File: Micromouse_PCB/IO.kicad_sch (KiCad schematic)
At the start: 22 parts, among them J4 Power, J5 ALARM, Q11 Q_NMOS_GSD, SW1 Slide switch, SW2 SW_Push, SW3 SW_Push

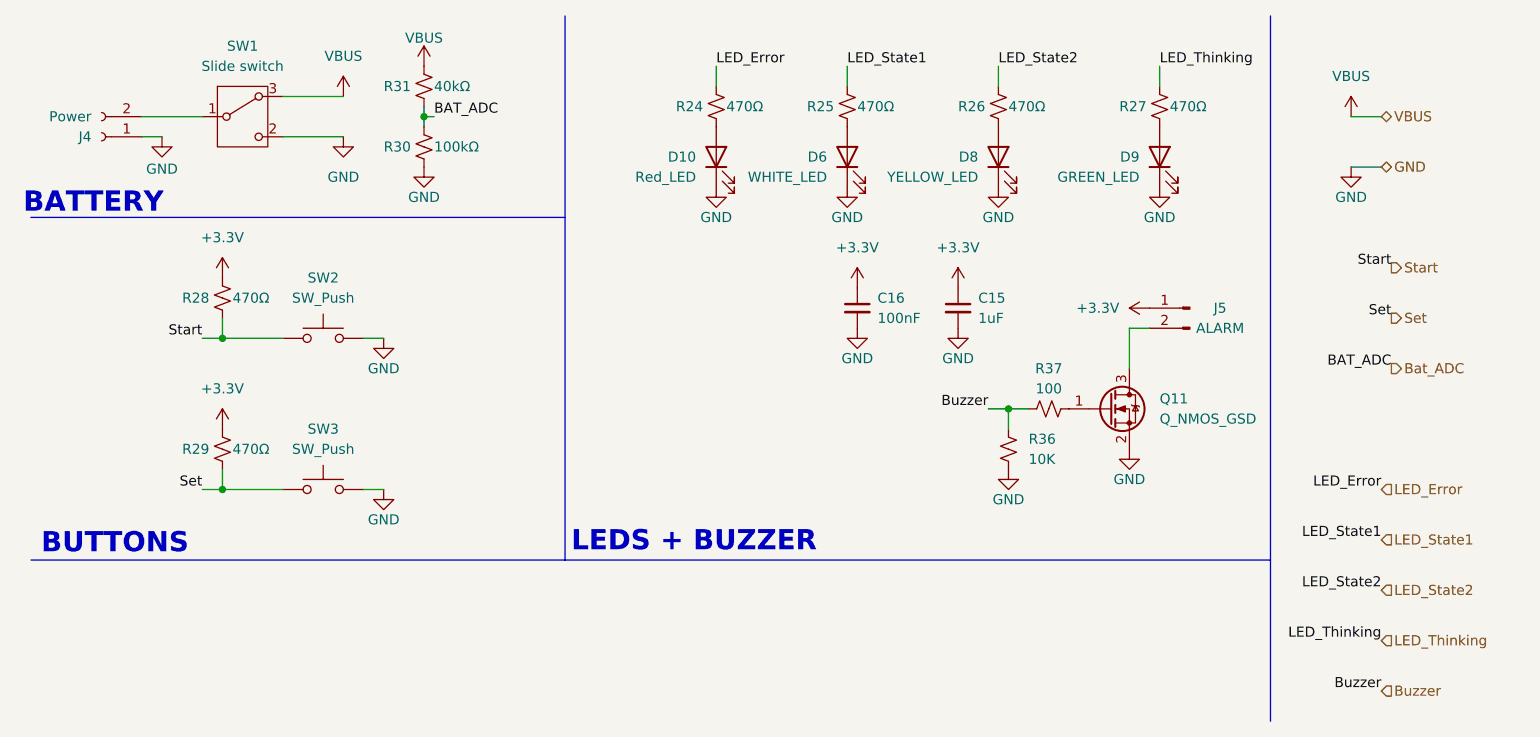
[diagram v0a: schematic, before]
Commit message: Schematic done
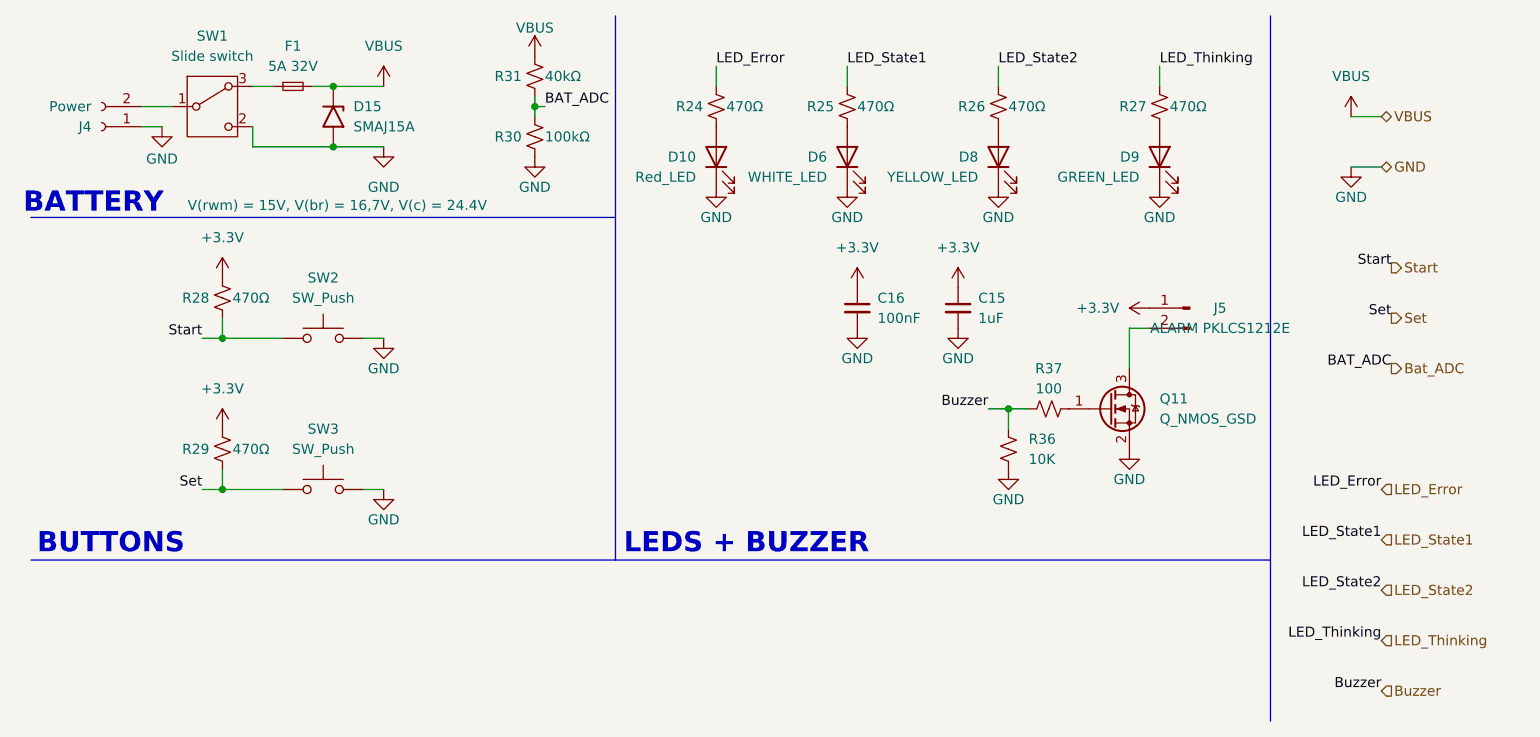
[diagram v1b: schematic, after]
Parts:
- added D15: SMAJ15A, Diode_SMD:D_SMA, symbol Diode:SMAJ15A
- added F1: 5A 32V, Fuse:Fuse_0603_1608Metric, symbol Device:Fuse_Small
- J5: value ALARM -> ALARM PKLCS1212E; Part # SMT-0540-S-R -> (none)
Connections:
- net GND: now also D15.2 (A2)
- net VBUS: now also D15.1 (A1), F1.2; no longer SW1.3 (A)
- new net: F1.1, SW1.3 (A)
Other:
- moved on the sheet: J4, R30, R31, SW1

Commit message: Placement 75% done on PCB
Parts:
- SW1: footprint UCIRP-KiCAD-Lib:Horizontal_Slide_Swiitch SK12D07VG4NSPA_CNK -> Button_Switch_THT:SW_Slide-03_Wuerth-WS-SLTV_10x2.5x6.4_P2.54mm
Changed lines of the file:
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@@
 			)
 		)
-		(property "Footprint" "UCIRP-KiCAD-Lib:Horizontal_Slide_Swiitch SK12D07VG4NSPA_CNK"
+		(property "Footprint" "Button_Switch_THT:SW_Slide-03_Wuerth-WS-SLTV_10x2.5x6.4_P2.54mm"
 			(at 35.56 34.29 0)
 			(effects

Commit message: PCB Done, need review now
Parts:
- J4: value Power -> Power XT30UPB-M; footprint Connector_AMASS:AMASS_XT30U-F_1x02_P5.0mm_Vertical -> Connector_AMASS:AMASS_XT30UPB-F_1x02_P5.0mm_Vertical
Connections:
- net +3.3V renamed +3V3
- net LED_Error renamed LED_Thinking1
- net LED_Thinking renamed LED_Thinking2
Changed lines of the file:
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@@
 		)
 	)
-	(label "LED_Thinking"
+	(label "LED_Thinking2"
 		(at 154.94 19.05 0)
 		(effects
@@
 		)
 	)
-	(label "LED_Thinking"
+	(label "LED_Thinking1"
+		(at 182.88 72.39 180)
+		(effects
+			(font
+				(size 1.27 1.27)
+			)
+			(justify right bottom)
+		)
+	)
+	(label "LED_Thinking2"
 		(at 182.88 91.44 180)
 		(effects
@@
 		)
 	)
-	(label "LED_Error"
-		(at 182.88 72.39 180)
-		(effects
-			(font
-				(size 1.27 1.27)
-			)
-			(justify right bottom)
-		)
-	)
 	(label "BAT_ADC"
 		(at 77.47 24.13 0)
@@
 		)
 	)
-	(label "LED_Error"
+	(label "LED_Thinking1"
 		(at 99.06 19.05 0)
 		(effects
@@
 		)
 	)
-	(hierarchical_label "LED_Thinking"
+	(hierarchical_label "LED_Thinking2"
 		(shape input)
 		(at 182.88 91.44 0)
@@
 		)
 	)
-	(hierarchical_label "LED_Error"
+	(hierarchical_label "LED_Thinking1"
 		(shape input)
 		(at 182.88 72.39 0)
@@
 		(on_board yes)
 		(dnp no)
-		(fields_autoplaced yes)
 		(property "Reference" "#PWR093"
 			(at 129.54 50.8 0)
@@
 			)
 		)
-		(property "Value" "+3.3V"
-			(at 129.54 41.91 0)
+		(property "Value" "+3V3"
+			(at 126.746 42.926 0)
 			(effects
 				(font
 					(size 1.27 1.27)
 				)
+				(justify left)
 			)
 		)
@@
 		(on_board yes)
 		(dnp no)
-		(fields_autoplaced yes)
 		(property "Reference" "#PWR099"
 			(at 36.83 49.53 0)
@@
 			)
 		)
-		(property "Value" "+3.3V"
-			(at 36.83 40.64 0)
+		(property "Value" "+3V3"
+			(at 33.782 41.91 0)
 			(effects
 				(font
 					(size 1.27 1.27)
 				)
+				(justify left)
 			)
 		)
@@
 		(on_board yes)
 		(dnp no)
-		(fields_autoplaced yes)
 		(property "Reference" "#PWR095"
 			(at 116.84 50.8 0)
@@
 			)
 		)
-		(property "Value" "+3.3V"
-			(at 116.84 41.91 0)
+		(property "Value" "+3V3"
+			(at 113.792 42.926 0)
 			(effects
 				(font
 					(size 1.27 1.27)
 				)
+				(justify left)
 			)
 		)
@@
 		(dnp no)
 		(property "Reference" "J5"
-			(at 162.56 49.53 0)
+			(at 162.306 41.402 0)
 			(effects
 				(font
@@
 		)
 		(property "Value" "ALARM PKLCS1212E"
-			(at 162.56 52.07 0)
+			(at 158.496 43.942 0)
 			(effects
 				(font
@@
 		(dnp no)
 		(property "Reference" "J4"
-			(at 20.32 26.6701 0)
+			(at 12.192 18.542 0)
 			(effects
 				(font
 					(size 1.27 1.27)
 				)
-				(justify left)
+				(justify right)
 			)
 		)
-		(property "Value" "Power"
-			(at 20.32 24.1301 0)
+		(property "Value" "Power XT30UPB-M"
+			(at 12.192 21.082 0)
 			(effects
 				(font
 					(size 1.27 1.27)
 				)
-				(justify left)
+				(justify right)
 			)
 		)
-		(property "Footprint" "Connector_AMASS:AMASS_XT30U-F_1x02_P5.0mm_Vertical"
+		(property "Footprint" "Connector_AMASS:AMASS_XT30UPB-F_1x02_P5.0mm_Vertical"
 			(at 21.59 26.67 0)
 			(effects
@@
 			)
 		)
-		(property "Datasheet" "https://jlcpcb.com/partdetail/Changzhou_AmassElec-XT30UM/C99101"
+		(property "Datasheet" "https://jlcpcb.com/partdetail/Changzhou_AmassElec-XT30UPBM/C428721"
 			(at 21.59 26.67 0)
 			(effects
@@
 		(on_board yes)
 		(dnp no)
-		(fields_autoplaced yes)
 		(property "Reference" "#PWR0100"
 			(at 36.83 68.58 0)
@@
 			)
 		)
-		(property "Value" "+3.3V"
-			(at 36.83 59.69 0)
+		(property "Value" "+3V3"
+			(at 33.782 60.706 0)
 			(effects
 				(font
 					(size 1.27 1.27)
 				)
+				(justify left)
 			)
 		)
@@
 		(on_board yes)
 		(dnp no)
-		(fields_autoplaced yes)
 		(property "Reference" "#PWR0154"
 			(at 157.48 49.53 0)
@@
 			)
 		)
-		(property "Value" "+3.3V"
-			(at 149.86 49.5299 90)
+		(property "Value" "+3V3"
+			(at 147.066 49.53 90)
 			(effects
 				(font
 					(size 1.27 1.27)
 				)
-				(justify left)
+				(justify right)
 			)
 		)

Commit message: Ordered
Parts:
- removed SW1: Slide switch, Button_Switch_THT:SW_Slide-03_Wuerth-WS-SLTV_10x2.5x6.4_P2.54mm, symbol Switch:SW_Wuerth_450301014042
- added SW1: SW_SPDT, Button_Switch_THT:SW_Slide_SPDT_Straight_CK_OS102011MS2Q, symbol Switch:SW_SPDT
- D9: value GREEN_LED -> Purple_LED
- Q11: value Q_NMOS_GSD -> DMG3402LQ
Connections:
- net GND: now also SW1.3 (C)
- net at F1.1: now also SW1.1 (A)
- net at J4.2 (Pin_2): now also SW1.2 (B)
